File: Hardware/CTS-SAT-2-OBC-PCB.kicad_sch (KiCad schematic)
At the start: 0 parts

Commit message: Add processor symbols to schematic
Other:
- added sheet RP2040 (RP2040.kicad_sch)
- added sheet STM32 (STM32.kicad_sch)
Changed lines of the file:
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@@
 	(generator "eeschema")
 	(generator_version "9.0")
-	(paper "A4")
+	(paper "A3")
+	(sheet
+		(at 35.56 36.83)
+		(size 64.77 62.23)
+		(exclude_from_sim no)
+		(in_bom yes)
+		(on_board yes)
+		(dnp no)
+		(fields_autoplaced yes)
+		(stroke
+			(width 0.1524)
+			(type solid)
+		)
+		(fill
+			(color 0 0 0 0.0000)
+		)
+		(property "Sheetname" "RP2040"
+			(at 35.56 36.1184 0)
+			(effects
+				(font
+					(size 1.27 1.27)
+				)
+				(justify left bottom)
+			)
+		)
+		(property "Sheetfile" "RP2040.kicad_sch"
+			(at 35.56 99.6446 0)
+			(effects
+				(font
+					(size 1.27 1.27)
+				)
+				(justify left top)
+			)
+		)
+		(instances
+			(project "CTS-SAT-2-OBC-PCB"
+				(path "/58243925-df8d-4fc1-899e-fce866d1d25a"
+					(page "2")
+				)
+			)
+		)
+	)
+	(sheet
+		(at 204.47 43.18)
+		(size 58.42 36.83)
+		(exclude_from_sim no)
+		(in_bom yes)
+		(on_board yes)
+		(dnp no)
+		(fields_autoplaced yes)
+		(stroke
+			(width 0.1524)
+			(type solid)
+		)
+		(fill
+			(color 0 0 0 0.0000)
+		)
+		(property "Sheetname" "STM32"
+			(at 204.47 42.4684 0)
+			(effects
+				(font
+					(size 1.27 1.27)
+				)
+				(justify left bottom)
+			)
+		)
+		(property "Sheetfile" "STM32.kicad_sch"
+			(at 204.47 80.5946 0)
+			(effects
+				(font
+					(size 1.27 1.27)
+				)
+				(justify left top)
+			)
+		)
+		(instances
+			(project "CTS-SAT-2-OBC-PCB"
+				(path "/58243925-df8d-4fc1-899e-fce866d1d25a"
+					(page "3")
+				)
+			)
+		)
+	)
 	(sheet_instances
 		(path "/"

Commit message: Connect RP2040, STM32, temperature sensor
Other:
- added sheet PC104 Header (PC104.kicad_sch)
- added sheet Temperature Sensor (temperature_sensor.kicad_sch)
- sheet RP2040 ports: added SPI0_CS0, SPI0_RX, SPI0_SCK, SPI0_TX; removed none
- sheet STM32 ports: added I2C4_SCL, I2C4_SDA, SPI2_MISO, SPI2_MOSI, SPI2_NCS, SPI2_SCK; removed none

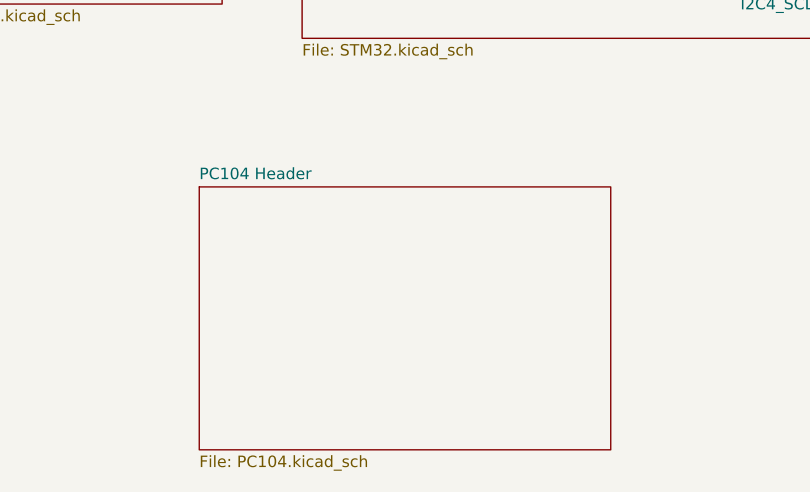
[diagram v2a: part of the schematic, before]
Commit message: Add PC104 header sub-schematic
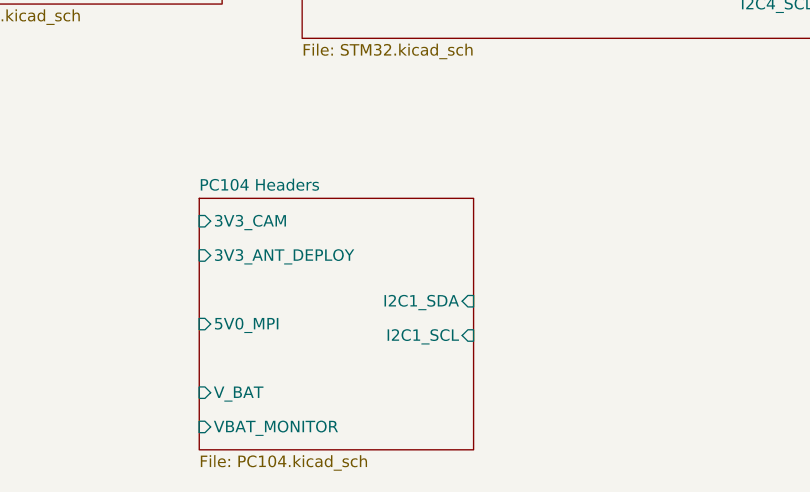
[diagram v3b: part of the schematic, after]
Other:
- sheet PC104 Header renamed PC104 Headers
- sheet PC104 Headers ports: added 3V3_ANT_DEPLOY, 3V3_CAM, 5V0_MPI, I2C1_SCL, I2C1_SDA, VBAT_MONITOR, V_BAT; removed none
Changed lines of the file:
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@@
 	)
 	(sheet
-		(at 193.04 96.52)
-		(size 45.72 29.21)
+		(at 193.04 97.79)
+		(size 30.48 27.94)
 		(exclude_from_sim no)
 		(in_bom yes)
@@
 			(color 0 0 0 0.0000)
 		)
-		(property "Sheetname" "PC104 Header"
-			(at 193.04 95.8084 0)
+		(property "Sheetname" "PC104 Headers"
+			(at 193.04 97.0784 0)
 			(effects
 				(font
@@
 			)
 		)
+		(pin "3V3_CAM" input
+			(at 193.04 100.33 180)
+			(effects
+				(font
+					(size 1.27 1.27)
+				)
+				(justify left)
+			)
+		)
+		(pin "I2C1_SDA" input
+			(at 223.52 109.22 0)
+			(effects
+				(font
+					(size 1.27 1.27)
+				)
+				(justify right)
+			)
+		)
+		(pin "5V0_MPI" input
+			(at 193.04 111.76 180)
+			(effects
+				(font
+					(size 1.27 1.27)
+				)
+				(justify left)
+			)
+		)
+		(pin "I2C1_SCL" input
+			(at 223.52 113.03 0)
+			(effects
+				(font
+					(size 1.27 1.27)
+				)
+				(justify right)
+			)
+		)
+		(pin "3V3_ANT_DEPLOY" input
+			(at 193.04 104.14 180)
+			(effects
+				(font
+					(size 1.27 1.27)
+				)
+				(justify left)
+			)
+		)
+		(pin "V_BAT" input
+			(at 193.04 119.38 180)
+			(effects
+				(font
+					(size 1.27 1.27)
+				)
+				(justify left)
+			)
+		)
+		(pin "VBAT_MONITOR" input
+			(at 193.04 123.19 180)
+			(effects
+				(font
+					(size 1.27 1.27)
+				)
+				(justify left)
+			)
+		)

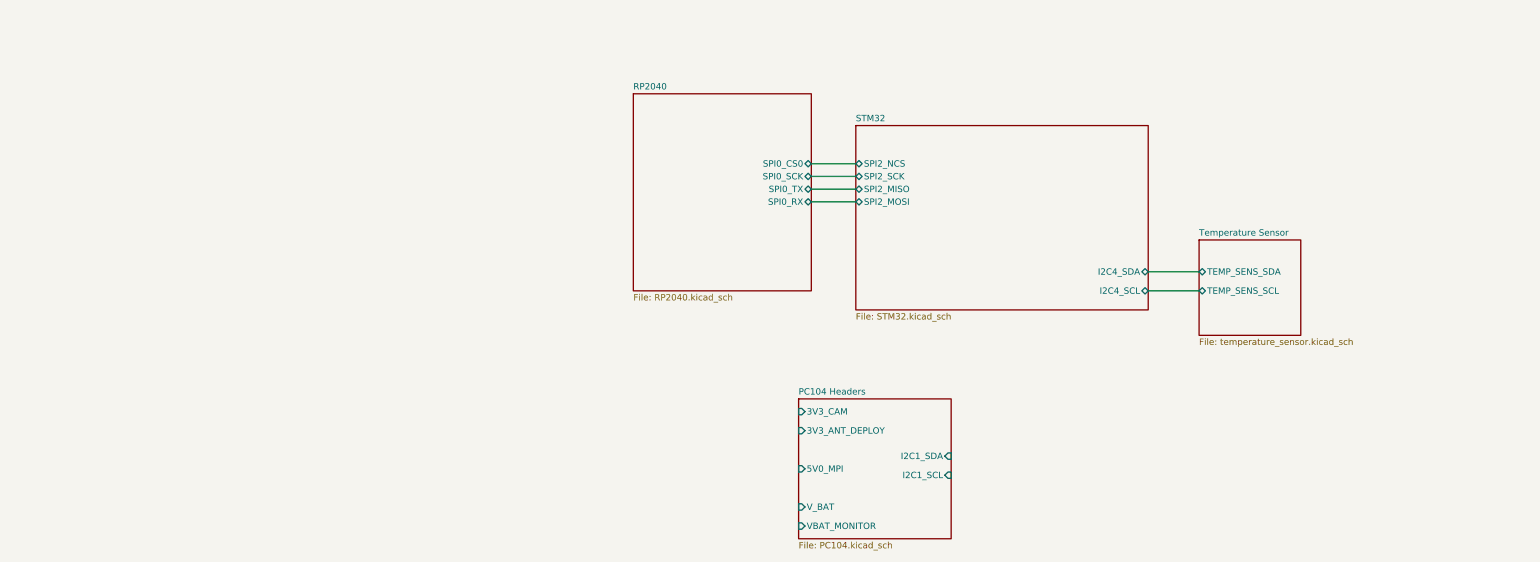
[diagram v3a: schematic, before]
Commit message: Add STM32 I2C and SPI connections
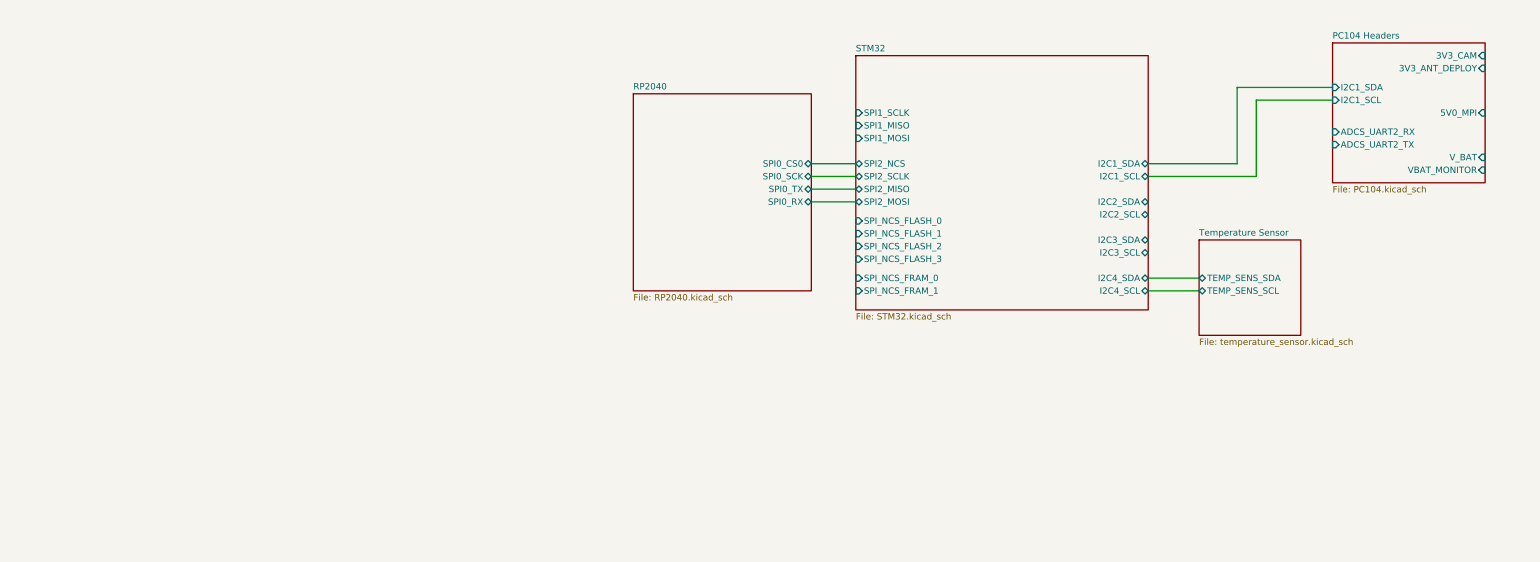
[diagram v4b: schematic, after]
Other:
- sheet PC104 Headers ports: added ADCS_UART2_RX, ADCS_UART2_TX; removed none
- sheet STM32 ports: added I2C1_SCL, I2C1_SDA, I2C2_SCL, I2C2_SDA, I2C3_SCL, I2C3_SDA, SPI1_MISO, SPI1_MOSI, SPI1_SCLK, SPI2_SCLK, SPI_NCS_FLASH_0, SPI_NCS_FLASH_1, SPI_NCS_FLASH_2, SPI_NCS_FLASH_3, SPI_NCS_FRAM_0, SPI_NCS_FRAM_1; removed SPI2_SCK

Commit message: Add UARTs to STM32
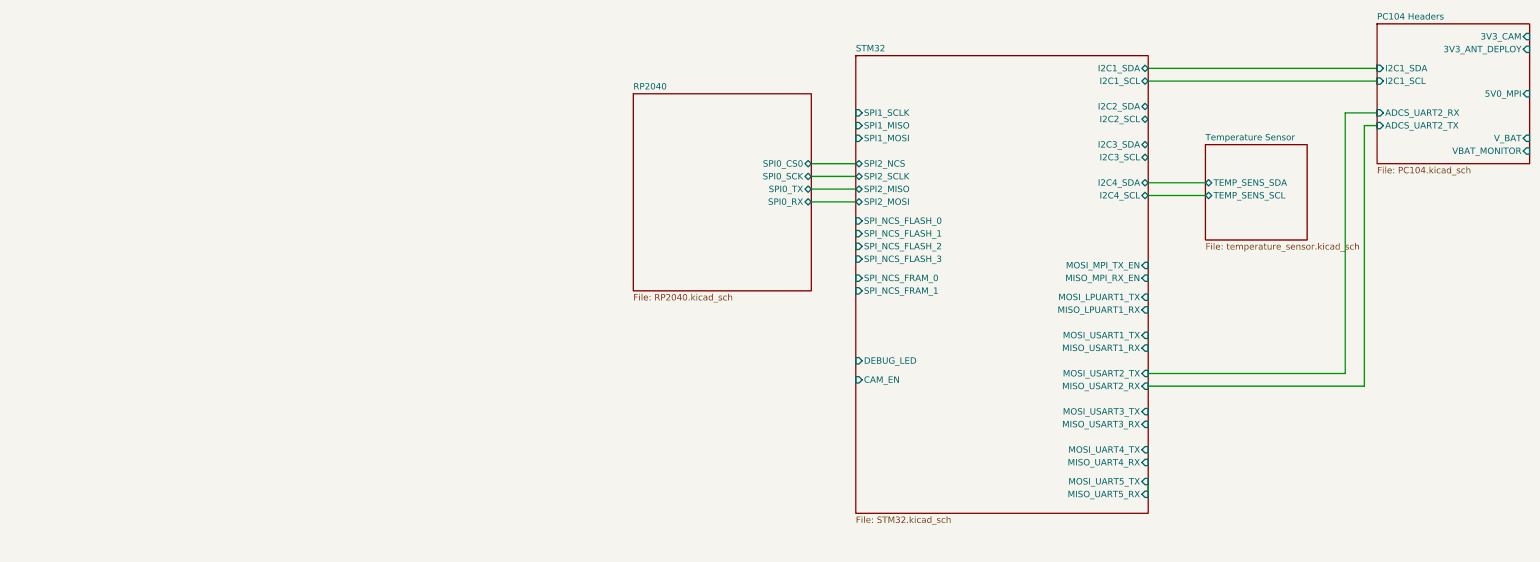
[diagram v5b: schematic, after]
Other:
- sheet STM32 ports: added CAM_EN, DEBUG_LED, MISO_LPUART1_RX, MISO_MPI_RX_EN, MISO_UART4_RX, MISO_UART5_RX, MISO_USART1_RX, MISO_USART2_RX, MISO_USART3_RX, MOSI_LPUART1_TX, MOSI_MPI_TX_EN, MOSI_UART4_TX, MOSI_UART5_TX, MOSI_USART1_TX, MOSI_USART2_TX, MOSI_USART3_TX; removed none
